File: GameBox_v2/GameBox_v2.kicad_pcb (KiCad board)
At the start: 2 copper layers, 35.5 x 75.5 mm, 18 parts, among them J1 OLED, SW1 SW_left, SW2 SW_up, SW3 SW_down, SW4 SW_right, SW5 ON/OFF, U1 ATmega328P-P, U2 3.3V_boost_regulator, Y1 16MHz

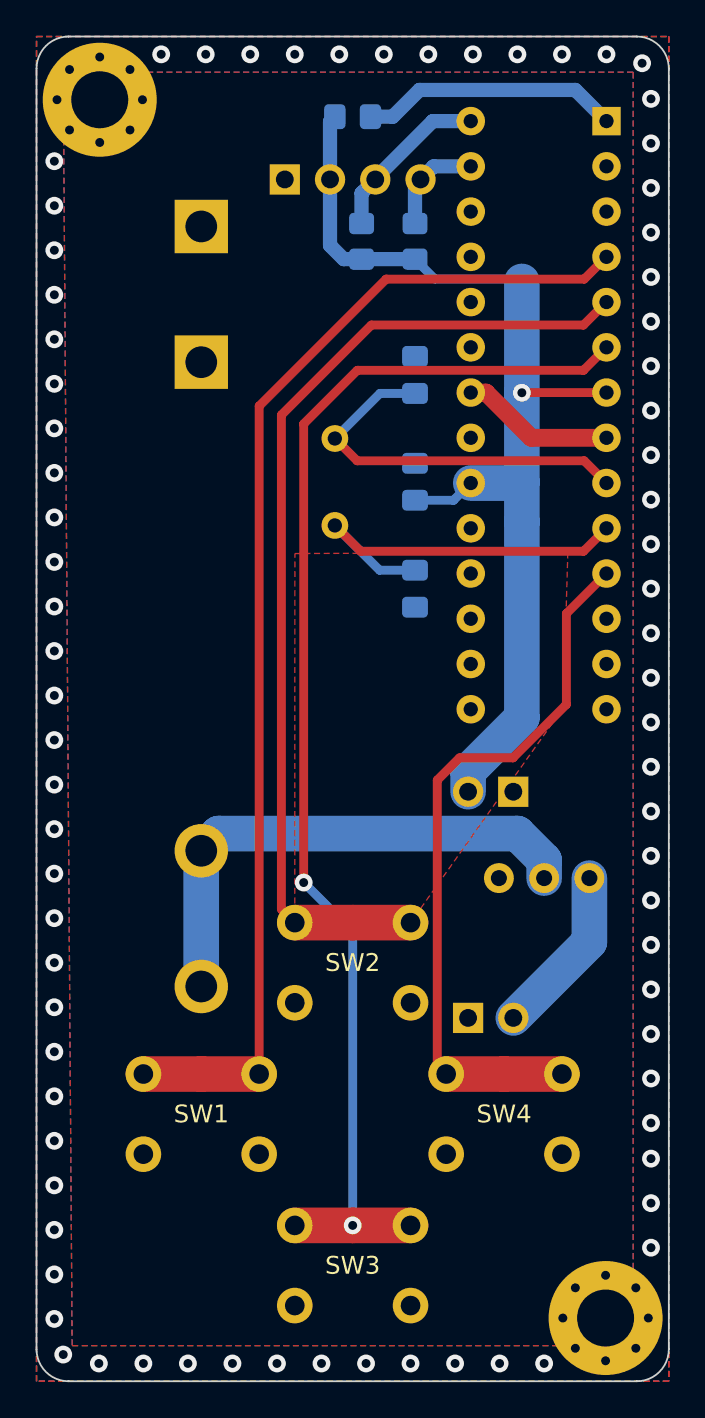
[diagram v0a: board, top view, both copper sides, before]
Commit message: Rounded tracks and teardrops
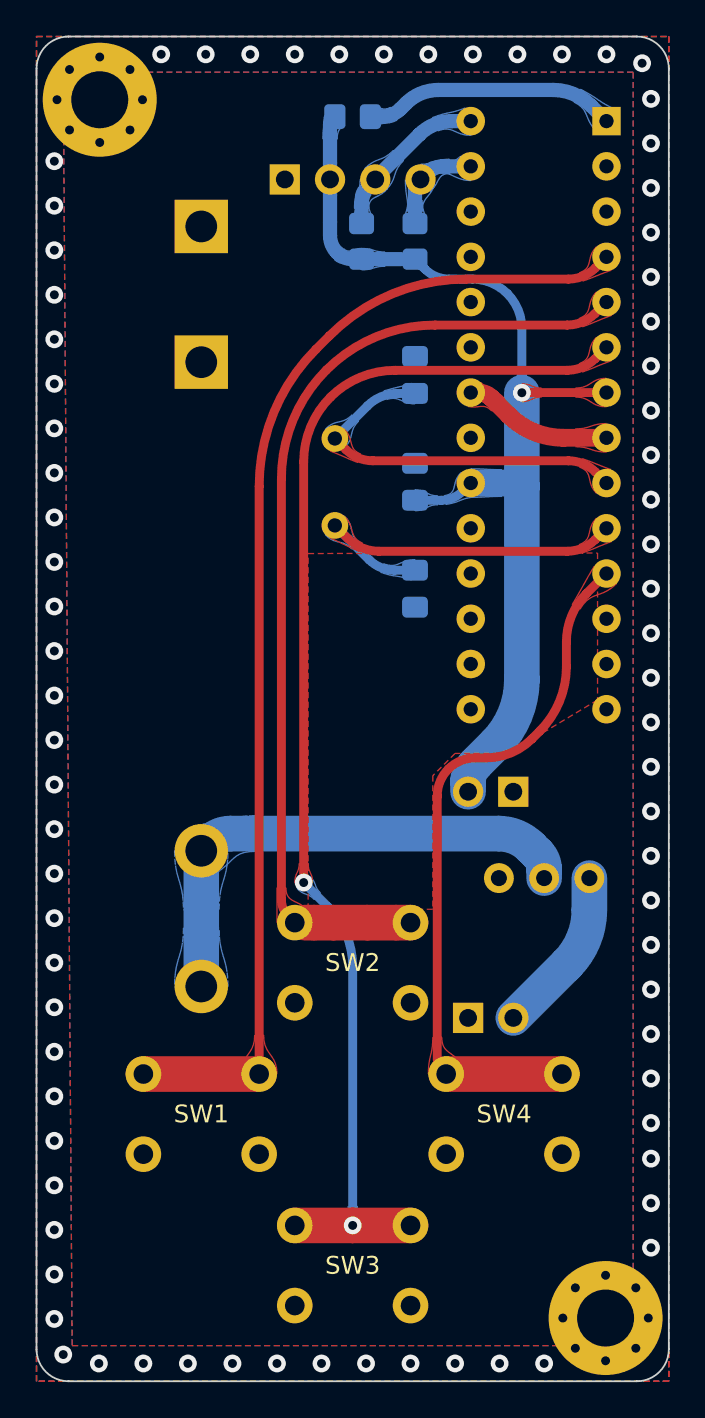
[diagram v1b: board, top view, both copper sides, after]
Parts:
- SW5: footprint GameBox:SS12D10 -> GameBox:SS12D00
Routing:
- net VCC: track 60.0 -> 58.2 mm
- net Net-(SW4-Pad1): track 40.5 -> 39.3 mm
- net Net-(SW1-Pad1): track 67.0 -> 65.8 mm
- net Net-(SW2-Pad1): track 56.2 -> 55.1 mm
- net Net-(SW3-Pad1): track 71.4 -> 70.6 mm

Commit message: Footprint updates
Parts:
- SW5: footprint GameBox:SS12D00 -> GameBox:EG1218
- moved SW5 1.25 mm to (177.5, 121.5)
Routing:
- net VDD: track 28.6 -> 28.0 mm
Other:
- board text added: "OFF/ON"
- board text removed: "ON/OFF"

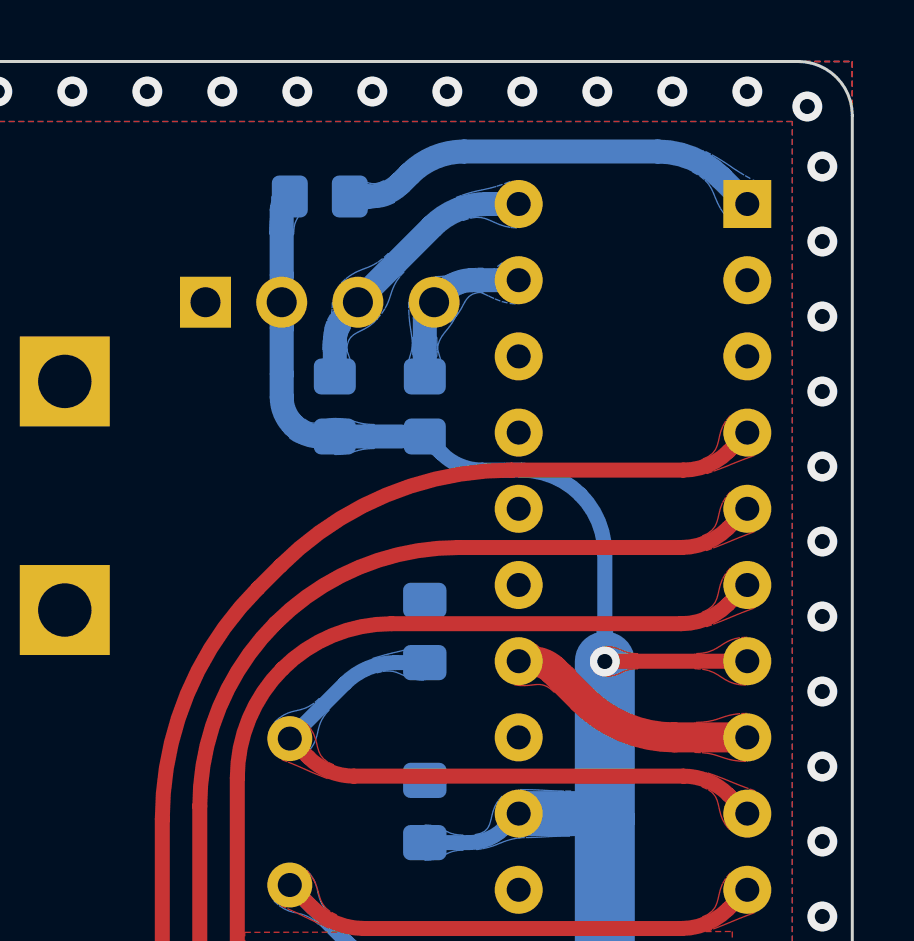
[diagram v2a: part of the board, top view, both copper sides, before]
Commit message: fixed OLEDs
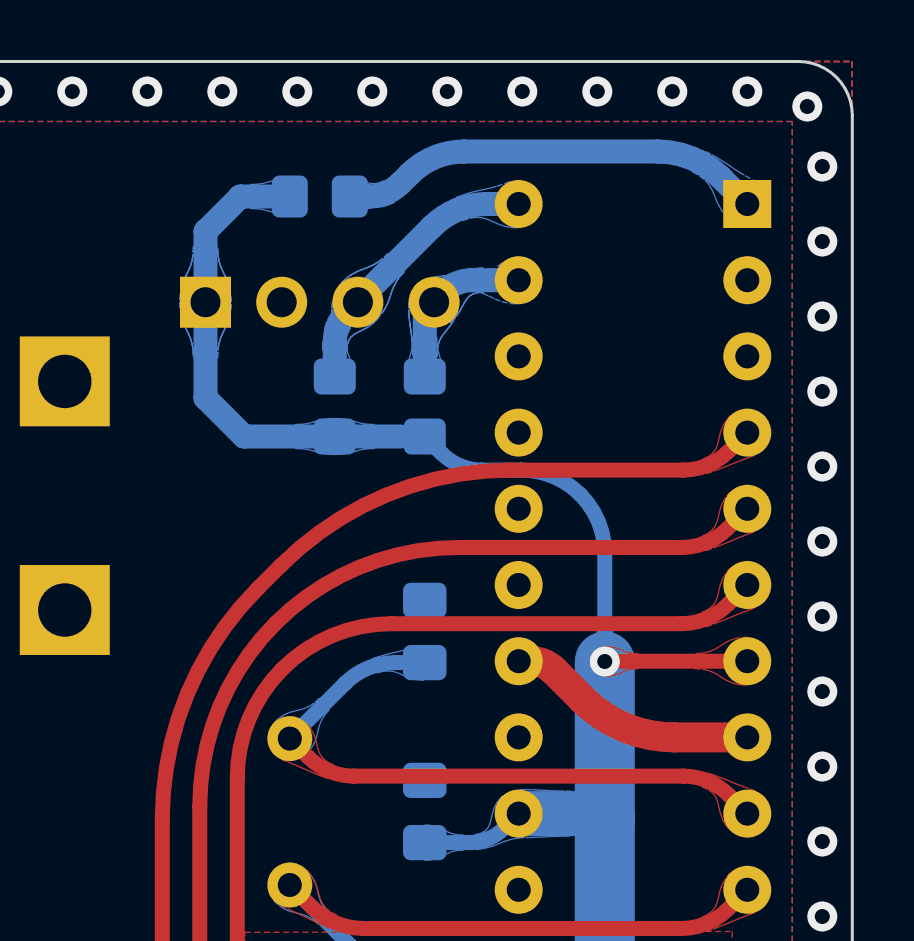
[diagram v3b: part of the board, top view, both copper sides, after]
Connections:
- J1 pad 1: GND -> VCC
- J1 pad 2: VCC -> GND
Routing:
- net VCC: track 58.2 -> 63.1 mm
